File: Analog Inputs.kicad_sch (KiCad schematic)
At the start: 0 parts

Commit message: Avance con el ADC para conectar al filtro para las celdas. Se debe realizar un excel para el cálculo del peso y cuadrar bien esa sección para que la programación sea lo más sencilla posible
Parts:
- added C10, C21, C39, C7: 10uF/50V, Resistor_SMD:R_1206_3216Metric_Pad1.30x1.75mm_HandSolder, symbol Device:C
- added C11, C13, C15, C23, C26, C31, C8: 100nF/50V, Resistor_SMD:R_0805_2012Metric_Pad1.20x1.40mm_HandSolder, symbol Device:C
- added C12, C19: 30pF/50V, Huella Capacitor_SMD:C_0603_1608Metric_Pad1.08x0.95mm_HandSolder 0 0 Centrado Centrado 0 0, symbol Device:C
- added C14, C16, C17: 1uF/50V, Resistor_SMD:R_0805_2012Metric_Pad1.20x1.40mm_HandSolder, symbol Device:C
- added C18, C9: 30pF/50V, Capacitor_SMD:C_0603_1608Metric_Pad1.08x0.95mm_HandSolder, symbol Device:C
- added R56, R57: 100, symbol Device:R
- added U10, U13: ADS1256, SSOP-28_5.3x10.2mm_P0.65mm, symbol LIB_SCH_CONTR:ADS1256
- added U11: REF35102QDBVR, Package_TO_SOT_SMD:SOT-23-6, symbol Reference_Voltage:REF35102QDBVR
- added Y2, Y3: 8.0Mhz, Crystal:Crystal_SMD_5032-2Pin_5.0x3.2mm, symbol Device:Crystal
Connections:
- new net: C19.2, U13.18 (XTAL2), Y3.1
- new net: C18.1, U13.19 (XTAL1/CLKIN), Y3.2
- new net: R56.2, U10.14 (~{SYNC}/~{PDWN}), U10.15 (~{RESET})
- new net: C12.2, U10.18 (XTAL2), Y2.1
- new net: C9.1, U10.19 (XTAL1/CLKIN), Y2.2
- new net: R57.2, U13.14 (~{SYNC}/~{PDWN}), U13.15 (~{RESET})
- new net: C17.1, U11.5 (NR)
- new net ADS1_CS: U10.20 (~{CS})
- new net ADS1_DRDY: U10.21 (~{DRDY})
- new net ADS1_MISO: U10.22 (DOUT)
- new net ADS1_MOSI: U10.23 (DIN)
- new net ADS1_SCLK: U10.24 (SCLK)
- new net ADS2_CS: U13.20 (~{CS})
- new net ADS2_DRDY: U13.21 (~{DRDY})
- new net ADS2_MISO: U13.22 (DOUT)
- new net ADS2_MOSI: U13.23 (DIN)
- new net ADS2_SCLK: U13.24 (SCLK)
- new net ADS_DIG_3V3: C21.1, C23.1, C7.1, C8.1, R56.1, R57.1, U10.16 (DVDD), U13.16 (DVDD)
- new net ADS_DIG_5V: C10.1, C11.1, C13.1, C16.1, C26.1, C39.1, U10.1 (AVDD), U11.3 (EN), U11.4 (VIN), U13.1 (AVDD)
- new net GND: C10.2, C11.2, C12.1, C13.2, C14.2, C15.2, C16.2, C17.2, C18.2, C19.1, C21.2, C23.2, C26.2, C31.2, C39.2, C7.2, C8.2, C9.2, U10.17 (DGND), U10.2 (AGND), U10.3 (VREFN), U11.1 (GND), U11.2 (GND), U13.17 (DGND), U13.2 (AGND), U13.3 (VREFN)
- new net REF: C14.1, C15.1, C31.1, U10.4 (VREFP), U11.6 (VREF), U13.4 (VREFP)
- no-connect marks 0 -> 10
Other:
- added sheet RC_Filter (LoadCell_Filter.kicad_sch)
- note added: "C115962"
- note added: "C13585"
- note added: "C1658"
- note added: "C28186"

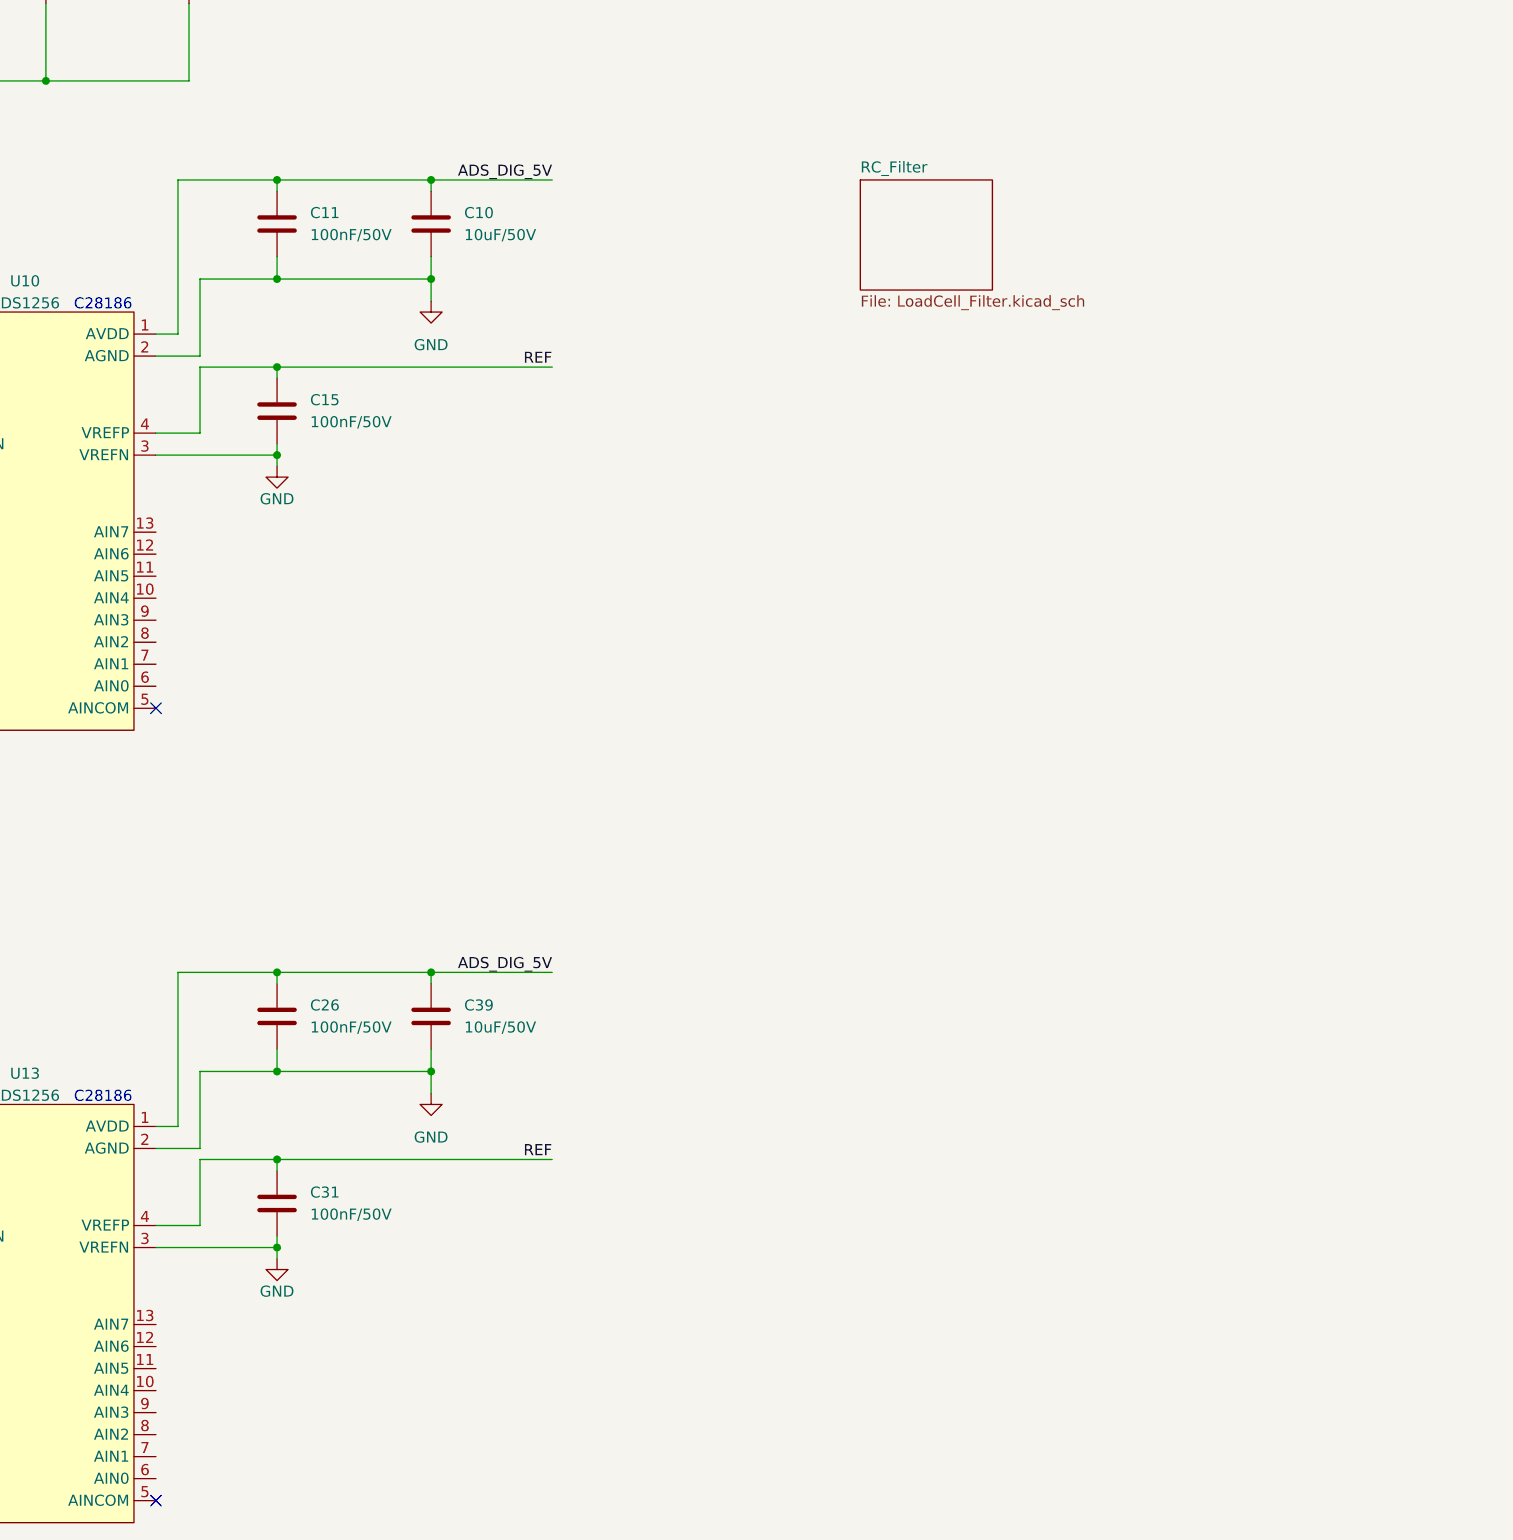
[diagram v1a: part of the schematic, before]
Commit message: Se culmina en que se utilizarà un filtro a  1.5khz para el sensor con divisor de 10k para la entrada ananaloga para el adc externo
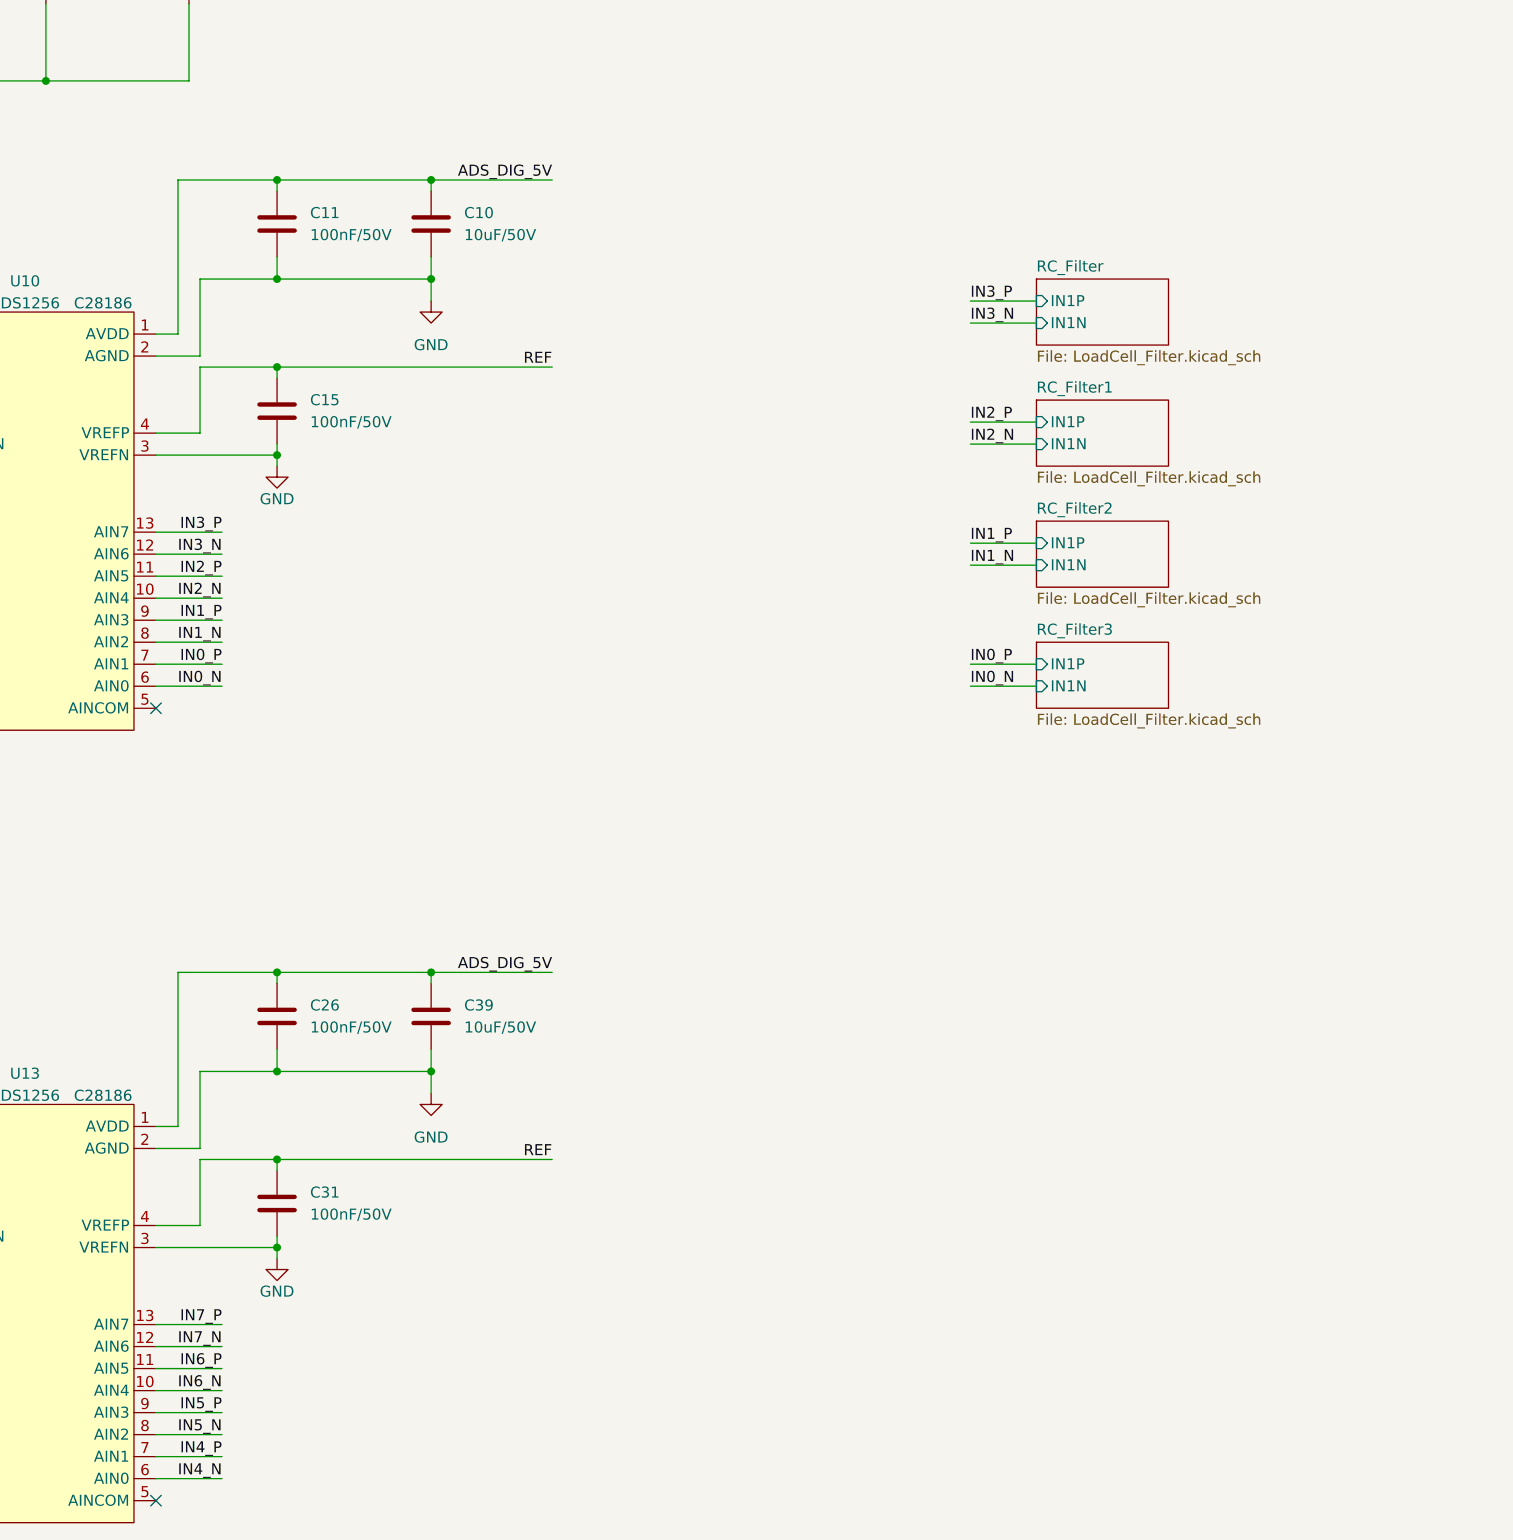
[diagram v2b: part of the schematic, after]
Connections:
- net IN6_N: now reaches U13.10 (AIN4)
- net IN6_P: now reaches U13.11 (AIN5)
- net IN7_N: now reaches U13.12 (AIN6)
- net IN7_P: now reaches U13.13 (AIN7)
- net IN4_N: now reaches U13.6 (AIN0)
- net IN4_P: now reaches U13.7 (AIN1)
- net IN5_N: now reaches U13.8 (AIN2)
- net IN5_P: now reaches U13.9 (AIN3)
- net IN2_N: now reaches U10.10 (AIN4)
- net IN2_P: now reaches U10.11 (AIN5)
- net IN3_N: now reaches U10.12 (AIN6)
- net IN3_P: now reaches U10.13 (AIN7)
- net IN0_N: now reaches U10.6 (AIN0)
- net IN0_P: now reaches U10.7 (AIN1)
- net IN1_N: now reaches U10.8 (AIN2)
- net IN1_P: now reaches U10.9 (AIN3)
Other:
- added sheet RC_Filter1 (LoadCell_Filter.kicad_sch)
- added sheet RC_Filter2 (LoadCell_Filter.kicad_sch)
- added sheet RC_Filter3 (LoadCell_Filter.kicad_sch)
- sheet RC_Filter ports: added IN1N, IN1P; removed none

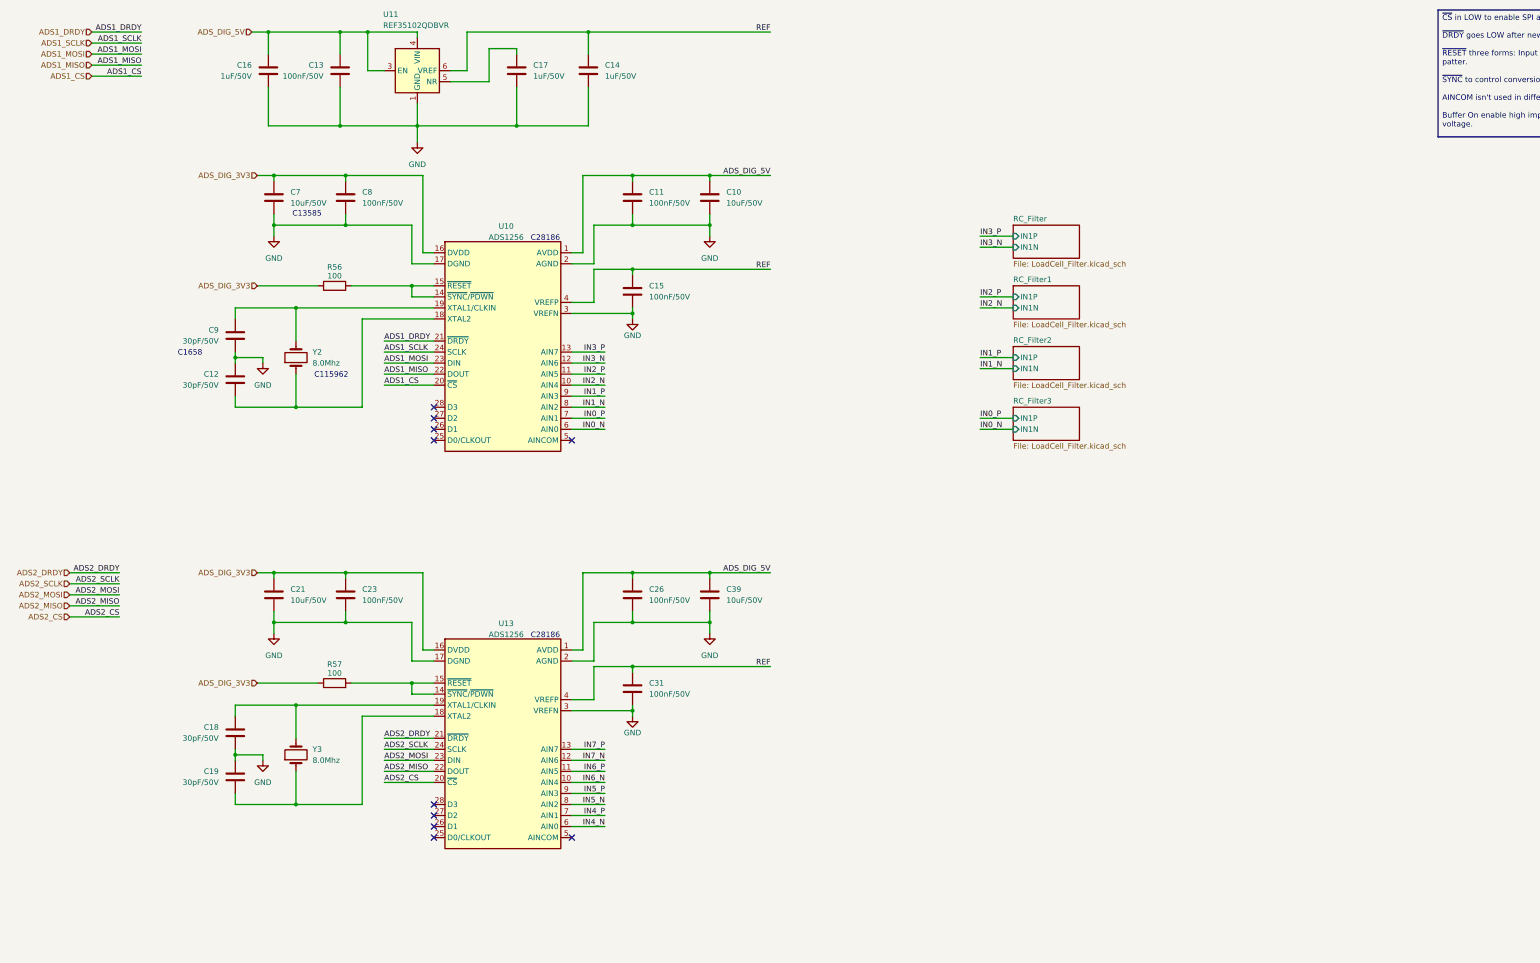
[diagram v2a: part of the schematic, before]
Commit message: Se termina el circuito de entrada análoga, se escoge la bornera. Se termina las salidas de rele, se asumen que se trabajara maximo a 220V y solo para activar contactores. El circuito para el sensor namur se esta realizando
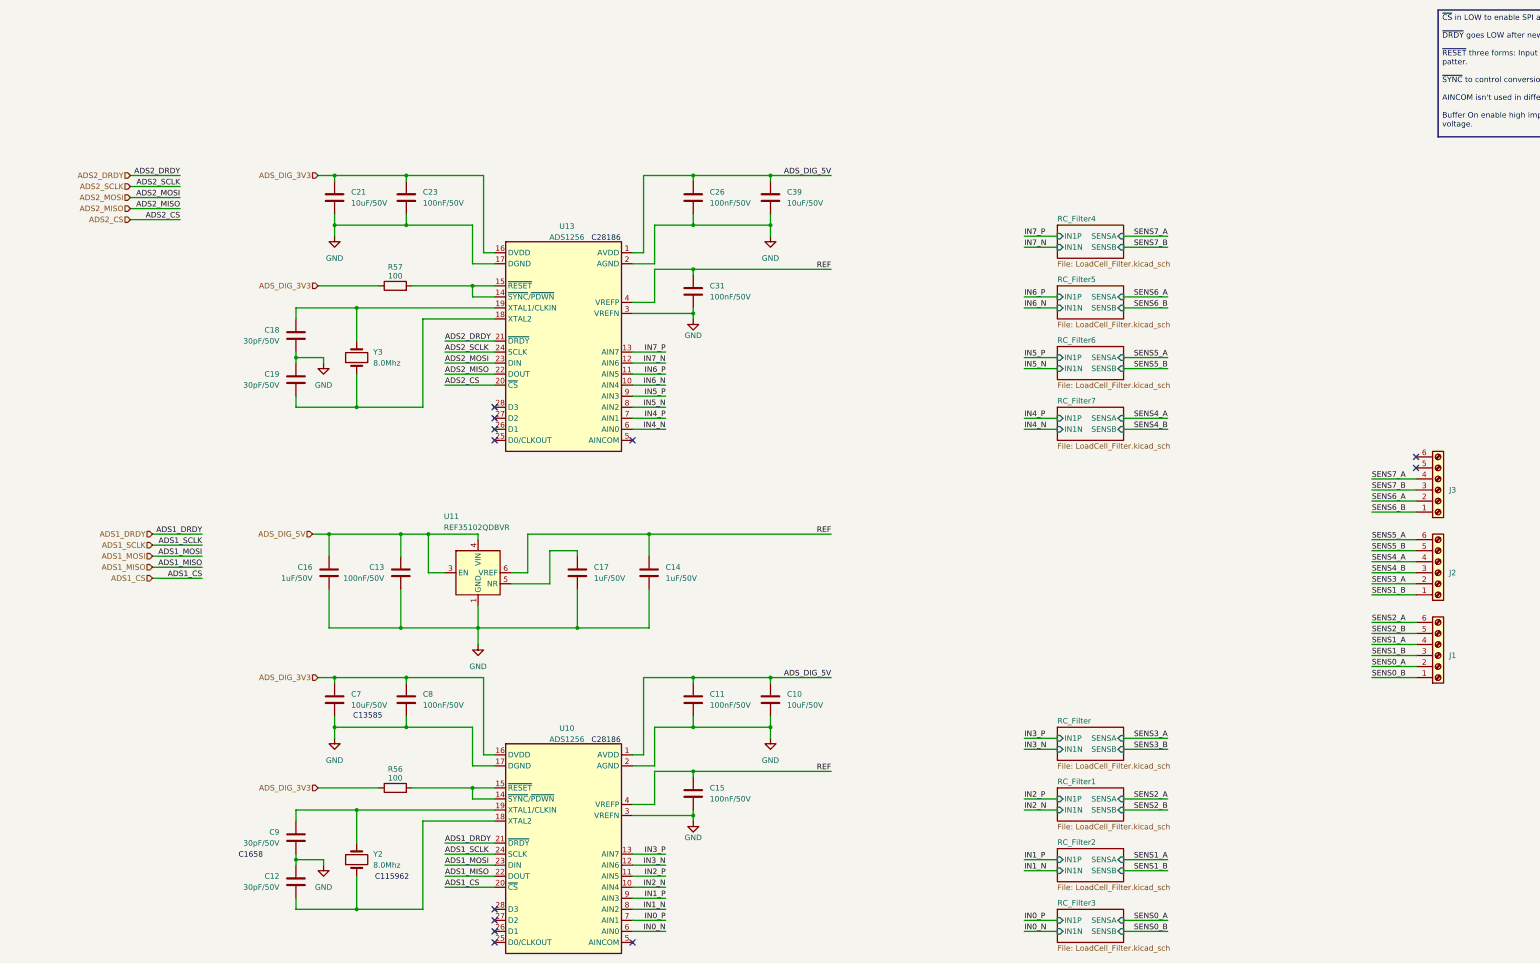
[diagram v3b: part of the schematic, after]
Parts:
- added J1, J2, J3: Screw_Terminal_01x06, LIB_PCB_CONT:15EDGRC_6P_3.81mm_Male-Rect_Degson, symbol Connector:Screw_Terminal_01x06
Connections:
- new net SENS0_A: J1.2 (Pin_2)
- new net SENS0_B: J1.1 (Pin_1)
- new net SENS1_A: J1.4 (Pin_4)
- new net SENS1_B: J1.3 (Pin_3), J2.1 (Pin_1)
- new net SENS2_A: J1.6 (Pin_6)
- new net SENS2_B: J1.5 (Pin_5)
- new net SENS3_A: J2.2 (Pin_2)
- new net SENS4_A: J2.4 (Pin_4)
- new net SENS4_B: J2.3 (Pin_3)
- new net SENS5_A: J2.6 (Pin_6)
- new net SENS5_B: J2.5 (Pin_5)
- new net SENS6_A: J3.2 (Pin_2)
- new net SENS6_B: J3.1 (Pin_1)
- new net SENS7_A: J3.4 (Pin_4)
- new net SENS7_B: J3.3 (Pin_3)
- no-connect marks 10 -> 12
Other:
- added sheet RC_Filter4 (LoadCell_Filter.kicad_sch)
- added sheet RC_Filter5 (LoadCell_Filter.kicad_sch)
- added sheet RC_Filter6 (LoadCell_Filter.kicad_sch)
- added sheet RC_Filter7 (LoadCell_Filter.kicad_sch)
- sheet RC_Filter ports: added SENSA, SENSB; removed none
- sheet RC_Filter1 ports: added SENSA, SENSB; removed none
- sheet RC_Filter2 ports: added SENSA, SENSB; removed none
- sheet RC_Filter3 ports: added SENSA, SENSB; removed none
- moved on the sheet: C10, C11, C12, C13, C14, C15, C16, C17, C18, C19, C21, C23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

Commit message: avance de pcb, se considera borneras externas para conexión de alimentación
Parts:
- removed C14: 1uF/50V, Resistor_SMD:R_0805_2012Metric_Pad1.20x1.40mm_HandSolder, symbol Device:C
- added C12: 1uF/50V, Resistor_SMD:R_0805_2012Metric_Pad1.20x1.40mm_HandSolder, symbol Device:C
- C1: renamed from C18; footprint Capacitor_SMD:C_0603_1608Metric_Pad1.08x0.95mm_HandSolder -> Capacitor_SMD:C_0603_1608Metric
- C2: renamed from C19; footprint Huella Capacitor_SMD:C_0603_1608Metric_Pad1.08x0.95mm_HandSolder 0 0 Centrado Centrado 0 0 -> Capacitor_SMD:C_0603_1608Metric
- C3: renamed from C9; footprint Capacitor_SMD:C_0603_1608Metric_Pad1.08x0.95mm_HandSolder -> Capacitor_SMD:C_0603_1608Metric
- C4: renamed from C12; footprint Huella Capacitor_SMD:C_0603_1608Metric_Pad1.08x0.95mm_HandSolder 0 0 Centrado Centrado 0 0 -> Capacitor_SMD:C_0603_1608Metric
- J10: renamed from J1; footprint LIB_PCB_CONT:15EDGRC_6P_3.81mm_Male-Rect_Degson -> LIB_PCB_CONT:15EDGVC_6P_3.81mm_Male-Vert_Degson
- J8: renamed from J3; footprint LIB_PCB_CONT:15EDGRC_6P_3.81mm_Male-Rect_Degson -> LIB_PCB_CONT:15EDGVC_6P_3.81mm_Male-Vert_Degson
- J9: renamed from J2; footprint LIB_PCB_CONT:15EDGRC_6P_3.81mm_Male-Rect_Degson -> LIB_PCB_CONT:15EDGVC_6P_3.81mm_Male-Vert_Degson
- R1: renamed from R57; footprint (none) -> Resistor_SMD:R_0603_1608Metric
- R2: renamed from R56; footprint (none) -> Resistor_SMD:R_0603_1608Metric
- U4: renamed from U13; footprint SSOP-28_5.3x10.2mm_P0.65mm -> Package_SO:SSOP-28_5.3x10.2mm_P0.65mm
- U5: renamed from U10; footprint SSOP-28_5.3x10.2mm_P0.65mm -> Package_SO:SSOP-28_5.3x10.2mm_P0.65mm
- renumbered C8 to C10, C17 to C11, C26 to C13, C31 to C14, C11 to C15, C15 to C16, C39 to C17, C10 to C18, C16 to C5, C21 to C6, C13 to C8, C23 to C9, U11 to U3, Y3 to Y1
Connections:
- net ADS2_MISO is gone; now on net ADS_MISO: U4.22 (DOUT)
- net ADS2_MOSI is gone; now on net ADS_MOSI: U4.23 (DIN)
- net ADS2_SCLK is gone; now on net ADS_SCLK: U4.24 (SCLK)
- net GND: now also J8.5 (Pin_5), C12.2
- net SENS1_B: no longer J9.1 (Pin_1)
- net SENS3_B: now also J9.1 (Pin_1)
- net 10V: now reaches J8.6 (Pin_6)
- net ADS1_MISO renamed ADS_MISO
- net ADS1_MOSI renamed ADS_MOSI
- net ADS1_SCLK renamed ADS_SCLK
- net REF renamed REF_2.5V
- net REF_2.5V: now also C12.1
- no-connect marks 12 -> 10
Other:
- moved on the sheet: C11, C5, C8, U3
